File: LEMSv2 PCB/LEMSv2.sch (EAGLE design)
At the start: 82 parts, among them J1 FEMALE 2x3, Q1 200mA/50V, Q10 200mA/50V, Q2 200mA/50V, Q4 MMBT3904, Q5 200mA/50V, Q6 MMBT3904, Q7 200mA/50V, Q8 MMBT3904, Q9 MMBT3904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

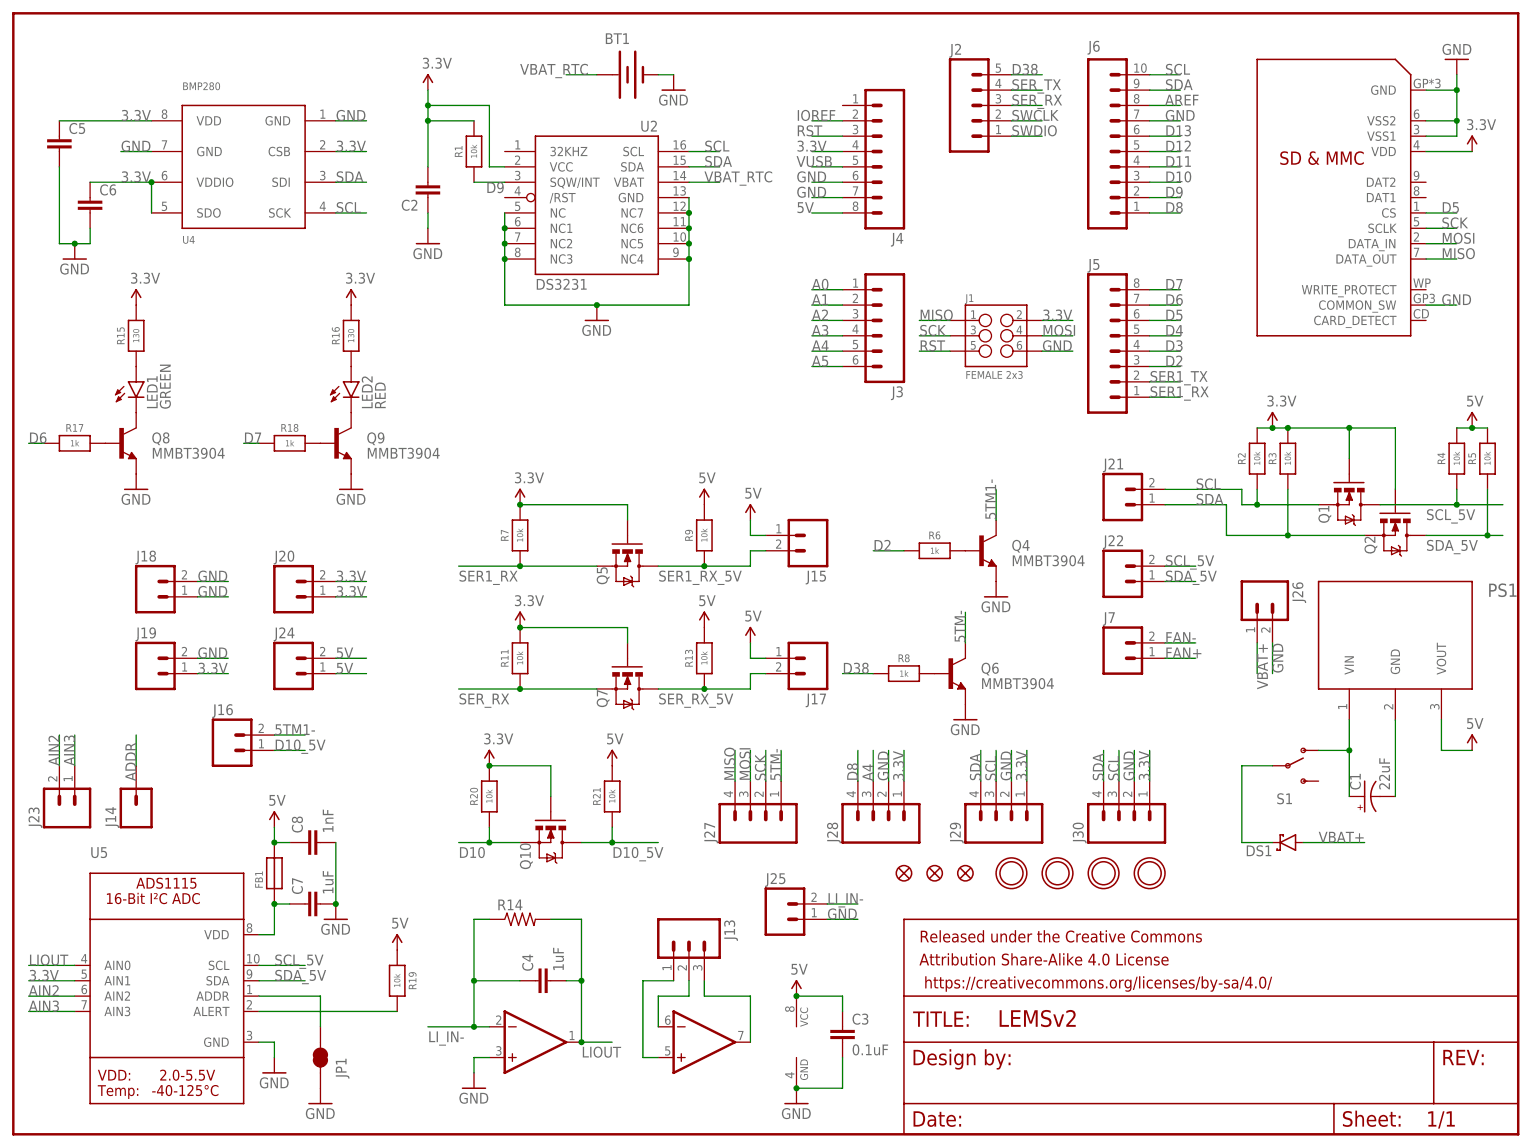
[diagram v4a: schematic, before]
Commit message: Started routing, part changes
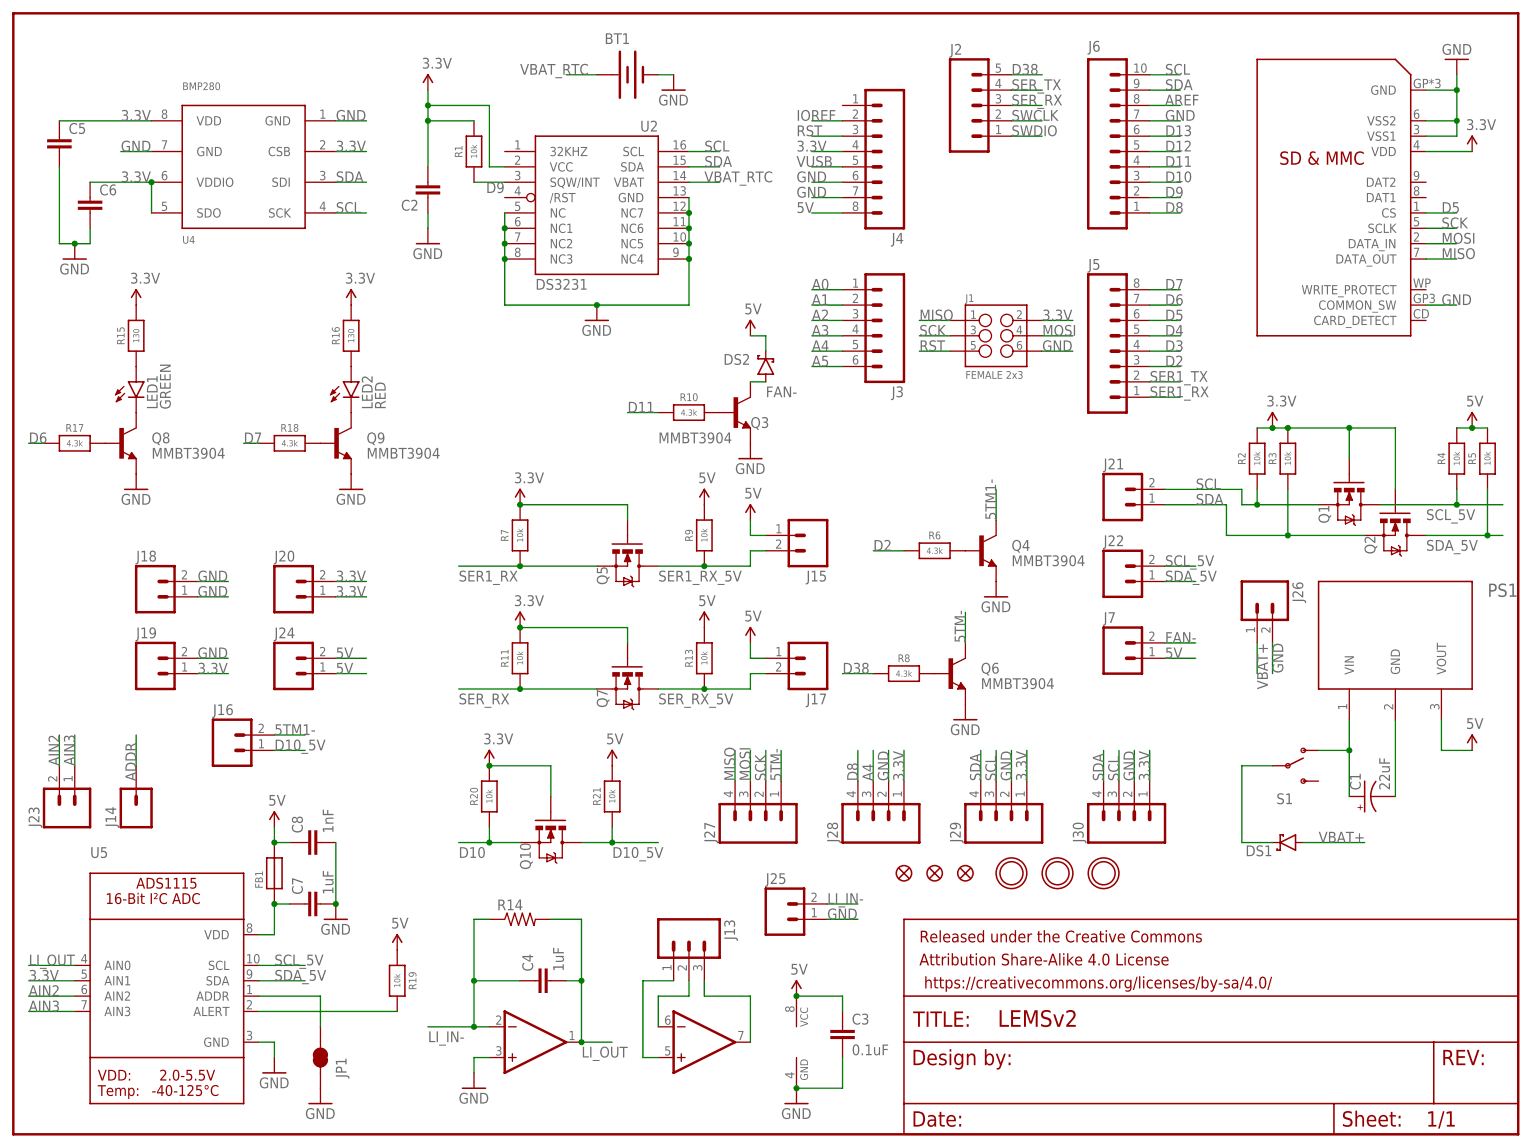
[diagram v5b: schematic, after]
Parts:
- removed U$4: MOUNTINGHOLE2.5, LEMSv2:MOUNTINGHOLE2.5
- added DS2: DIODE_SCHOTTKY, LEMSv2:DIODE_SCHOTTKY
- added Q3: MMBT3904, LEMSv2:MMBT3904
- added R10: 4.3k, LEMSv2:RESISTOR_0805
- R17, R18, R6, R8: value 1k -> 4.3k
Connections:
- net LIOUT renamed LI_OUT
- removed net FAN+: J7.1
- new net N$15: Q3.B, R10.2
- net 5V: now also DS2.C, J7.1
- net D11: now also R10.1
- net FAN-: now also DS2.A, Q3.C
- net GND: now also Q3.E
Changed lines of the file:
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@@
 <part name="U$2" library="LEMSv2" deviceset="MOUNTINGHOLE" device="2.5"/>
 <part name="U$3" library="LEMSv2" deviceset="MOUNTINGHOLE" device="2.5"/>
-<part name="U$4" library="LEMSv2" deviceset="MOUNTINGHOLE" device="2.5"/>
 <part name="C3" library="LEMSv2" deviceset="CAP" device="" value="0.1uF"/>
 <part name="U3" library="LEMSv2" deviceset="TLV2372" device=""/>
@@
 <part name="R15" library="LEMSv2" deviceset="RESISTOR" device="_0805" value="130"/>
 <part name="R16" library="LEMSv2" deviceset="RESISTOR" device="_0805" value="130"/>
-<part name="R17" library="LEMSv2" deviceset="RESISTOR" device="_0805" value="1k"/>
-<part name="R18" library="LEMSv2" deviceset="RESISTOR" device="_0805" value="1k"/>
+<part name="R17" library="LEMSv2" deviceset="RESISTOR" device="_0805" value="4.3k"/>
+<part name="R18" library="LEMSv2" deviceset="RESISTOR" device="_0805" value="4.3k"/>
 <part name="LED1" library="LEMSv2" deviceset="LED_GREEN" device="" value="GREEN"/>
 <part name="LED2" library="LEMSv2" deviceset="LED_RED" device="" value="RED"/>
@@
 <part name="Q4" library="LEMSv2" deviceset="MMBT3904" device=""/>
 <part name="Q6" library="LEMSv2" deviceset="MMBT3904" device=""/>
-<part name="R6" library="LEMSv2" deviceset="RESISTOR" device="_0805" value="1k"/>
-<part name="R8" library="LEMSv2" deviceset="RESISTOR" device="_0805" value="1k"/>
+<part name="R6" library="LEMSv2" deviceset="RESISTOR" device="_0805" value="4.3k"/>
+<part name="R8" library="LEMSv2" deviceset="RESISTOR" device="_0805" value="4.3k"/>
 <part name="SUPPLY17" library="LEMSv2" deviceset="5V" device=""/>
 <part name="SUPPLY18" library="LEMSv2" deviceset="5V" device=""/>
@@
 <part name="GND14" library="LEMSv2" deviceset="GND" device=""/>
 <part name="DS1" library="LEMSv2" deviceset="DIODE_SCHOTTKY" device=""/>
+<part name="DS2" library="LEMSv2" deviceset="DIODE_SCHOTTKY" device=""/>
+<part name="Q3" library="LEMSv2" deviceset="MMBT3904" device=""/>
+<part name="R10" library="LEMSv2" deviceset="RESISTOR" device="_0805" value="4.3k"/>
+<part name="GND15" library="LEMSv2" deviceset="GND" device=""/>
+<part name="SUPPLY19" library="LEMSv2" deviceset="5V" device=""/>
 </parts>
 <sheets>
@@
 <instance part="U$2" gate="G$1" x="172.72" y="43.18"/>
 <instance part="U$3" gate="G$1" x="180.34" y="43.18"/>
-<instance part="U$4" gate="G$1" x="187.96" y="43.18"/>
 <instance part="C3" gate="G$1" x="137.16" y="15.24"/>
 <instance part="U3" gate="TLV2372-1" x="83.82" y="15.24" smashed="yes"/>
@@
 <attribute name="NAME" x="208.28" y="47.7774" size="1.778" layer="95" rot="R180"/>
 </instance>
+<instance part="DS2" gate="G$1" x="124.46" y="127" smashed="yes" rot="R90">
+<attribute name="NAME" x="121.92" y="129.0574" size="1.778" layer="95" rot="R180"/>
+</instance>
+<instance part="Q3" gate="G$1" x="119.38" y="119.38" smashed="yes">
+<attribute name="NAME" x="121.92" y="116.84" size="1.778" layer="95"/>
+<attribute name="VALUE" x="106.68" y="114.3" size="1.778" layer="96"/>
+</instance>
+<instance part="R10" gate="G$1" x="111.76" y="119.38"/>
+<instance part="GND15" gate="1" x="121.92" y="111.76"/>
+<instance part="SUPPLY19" gate="G$1" x="121.92" y="132.08"/>
 </instances>
 <busses>
@@
 <label x="208.28" y="81.28" size="1.778" layer="95" rot="R270"/>
 </segment>
+<segment>
+<pinref part="Q3" gate="G$1" pin="E"/>
+<pinref part="GND15" gate="1" pin="GND"/>
+</segment>
 </net>
 <net name="SCK" class="0">
@@
 <wire x1="121.92" y1="81.28" x2="121.92" y2="78.74" width="0.1524" layer="91"/>
 <wire x1="121.92" y1="78.74" x2="124.46" y2="78.74" width="0.1524" layer="91"/>
+</segment>
+<segment>
+<pinref part="DS2" gate="G$1" pin="C"/>
+<wire x1="124.46" y1="129.54" x2="124.46" y2="132.08" width="0.1524" layer="91"/>
+<wire x1="124.46" y1="132.08" x2="121.92" y2="132.08" width="0.1524" layer="91"/>
+<pinref part="SUPPLY19" gate="G$1" pin="5V"/>
+</segment>
+<segment>
+<pinref part="J7" gate="G$1" pin="1"/>
+<wire x1="190.5" y1="78.74" x2="195.58" y2="78.74" width="0.1524" layer="91"/>
+<label x="190.5" y="78.74" size="1.778" layer="95"/>
 </segment>
 </net>
@@
 <label x="190.5" y="160.02" size="1.778" layer="95"/>
 </segment>
+<segment>
+<pinref part="R10" gate="G$1" pin="1"/>
+<wire x1="106.68" y1="119.38" x2="101.6" y2="119.38" width="0.1524" layer="91"/>
+<label x="101.6" y="119.38" size="1.778" layer="95"/>
+</segment>
 </net>
 <net name="D10" class="0">
@@
 </segment>
 </net>
-<net name="LIOUT" class="0">
+<net name="LI_OUT" class="0">
 <segment>
 <pinref part="U3" gate="TLV2372-1" pin="OUT"/>
@@
 <label x="190.5" y="81.28" size="1.778" layer="95"/>
 </segment>
-</net>
-<net name="FAN+" class="0">
-<segment>
-<pinref part="J7" gate="G$1" pin="1"/>
-<wire x1="190.5" y1="78.74" x2="195.58" y2="78.74" width="0.1524" layer="91"/>
-<label x="190.5" y="78.74" size="1.778" layer="95"/>
+<segment>
+<pinref part="Q3" gate="G$1" pin="C"/>
+<pinref part="DS2" gate="G$1" pin="A"/>
+<wire x1="121.92" y1="124.46" x2="124.46" y2="124.46" width="0.1524" layer="91"/>
+<label x="124.46" y="121.92" size="1.778" layer="95"/>
 </segment>
 </net>
@@
 </segment>
 </net>
+<net name="N$15" class="0">
+<segment>
+<pinref part="Q3" gate="G$1" pin="B"/>
+<pinref part="R10" gate="G$1" pin="2"/>
+</segment>
+</net>

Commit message: More routing
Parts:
- C2: value (none) -> 1uF
- C5, C6: value (none) -> 0.1uF
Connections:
- new net RST2: J1.5
- net 5TM-: now also J17.2; no longer J27.1
- net D11: no longer R10.1
- net D4: now also R10.1
- net RST: no longer J1.5
- net SER_RX_5V: now also J27.1; no longer J17.2
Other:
- moved on the sheet: J15, J17
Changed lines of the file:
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@@
 <part name="C1" library="LEMSv2" deviceset="CAP_POL" device="PTH2" value="22uF"/>
 <part name="SUPPLY2" library="SparkFun-Aesthetics" deviceset="5V" device=""/>
-<part name="C2" library="LEMSv2" deviceset="CAP" device=""/>
+<part name="C2" library="LEMSv2" deviceset="CAP" device="" value="1uF"/>
 <part name="GND1" library="LEMSv2" deviceset="GND" device=""/>
 <part name="SUPPLY3" library="LEMSv2" deviceset="3.3V" device=""/>
@@
 <part name="R14" library="adafruit" deviceset="R-US_" device="FLIPFLOP"/>
 <part name="U4" library="LEMSv2" deviceset="BMP280" device=""/>
-<part name="C5" library="LEMSv2" deviceset="CAP" device=""/>
-<part name="C6" library="LEMSv2" deviceset="CAP" device=""/>
+<part name="C5" library="LEMSv2" deviceset="CAP" device="" value="0.1uF"/>
+<part name="C6" library="LEMSv2" deviceset="CAP" device="" value="0.1uF"/>
 <part name="GND7" library="LEMSv2" deviceset="GND" device=""/>
 <part name="Q8" library="LEMSv2" deviceset="MMBT3904" device=""/>
@@
 <instance part="GND12" gate="1" x="50.8" y="5.08"/>
 <instance part="SUPPLY14" gate="G$1" x="63.5" y="30.48"/>
-<instance part="J15" gate="G$1" x="132.08" y="99.06" rot="R180"/>
+<instance part="J15" gate="G$1" x="132.08" y="96.52" rot="R180"/>
 <instance part="J16" gate="G$1" x="35.56" y="63.5"/>
-<instance part="J17" gate="G$1" x="132.08" y="78.74" rot="R180"/>
+<instance part="J17" gate="G$1" x="152.4" y="111.76" rot="R180"/>
 <instance part="J18" gate="G$1" x="22.86" y="88.9"/>
 <instance part="J19" gate="G$1" x="22.86" y="76.2"/>
@@
 <instance part="R6" gate="G$1" x="152.4" y="96.52"/>
 <instance part="R8" gate="G$1" x="147.32" y="76.2"/>
-<instance part="SUPPLY17" gate="G$1" x="121.92" y="101.6"/>
-<instance part="SUPPLY18" gate="G$1" x="121.92" y="81.28"/>
+<instance part="SUPPLY17" gate="G$1" x="124.46" y="99.06"/>
+<instance part="SUPPLY18" gate="G$1" x="142.24" y="111.76"/>
 <instance part="GND13" gate="1" x="162.56" y="88.9"/>
 <instance part="GND14" gate="1" x="157.48" y="68.58"/>
@@
 <label x="129.54" y="165.1" size="1.778" layer="95"/>
 </segment>
-<segment>
-<pinref part="J1" gate="G$1" pin="5"/>
-<wire x1="154.94" y1="129.54" x2="149.86" y2="129.54" width="0.1524" layer="91"/>
-<label x="149.86" y="129.54" size="1.778" layer="95"/>
-</segment>
 </net>
 <net name="VUSB" class="0">
@@
 <pinref part="SUPPLY17" gate="G$1" pin="5V"/>
 <pinref part="J15" gate="G$1" pin="1"/>
-<wire x1="121.92" y1="101.6" x2="121.92" y2="99.06" width="0.1524" layer="91"/>
-<wire x1="121.92" y1="99.06" x2="124.46" y2="99.06" width="0.1524" layer="91"/>
+<wire x1="124.46" y1="99.06" x2="124.46" y2="96.52" width="0.1524" layer="91"/>
 </segment>
 <segment>
 <pinref part="SUPPLY18" gate="G$1" pin="5V"/>
 <pinref part="J17" gate="G$1" pin="1"/>
-<wire x1="121.92" y1="81.28" x2="121.92" y2="78.74" width="0.1524" layer="91"/>
-<wire x1="121.92" y1="78.74" x2="124.46" y2="78.74" width="0.1524" layer="91"/>
+<wire x1="142.24" y1="111.76" x2="144.78" y2="111.76" width="0.1524" layer="91"/>
 </segment>
 <segment>
@@
 <label x="190.5" y="160.02" size="1.778" layer="95"/>
 </segment>
-<segment>
-<pinref part="R10" gate="G$1" pin="1"/>
-<wire x1="106.68" y1="119.38" x2="101.6" y2="119.38" width="0.1524" layer="91"/>
-<label x="101.6" y="119.38" size="1.778" layer="95"/>
-</segment>
 </net>
 <net name="D10" class="0">
@@
 <label x="190.5" y="132.08" size="1.778" layer="95"/>
 </segment>
+<segment>
+<pinref part="R10" gate="G$1" pin="1"/>
+<wire x1="106.68" y1="119.38" x2="101.6" y2="119.38" width="0.1524" layer="91"/>
+<label x="101.6" y="119.38" size="1.778" layer="95"/>
+</segment>
 </net>
 <net name="D3" class="0">
@@
 <wire x1="106.68" y1="93.98" x2="114.3" y2="93.98" width="0.1524" layer="91"/>
 <pinref part="R9" gate="G$1" pin="1"/>
-<wire x1="114.3" y1="93.98" x2="121.92" y2="93.98" width="0.1524" layer="91"/>
+<wire x1="114.3" y1="93.98" x2="124.46" y2="93.98" width="0.1524" layer="91"/>
 <junction x="114.3" y="93.98"/>
 <label x="106.68" y="91.44" size="1.778" layer="95"/>
-<wire x1="121.92" y1="93.98" x2="121.92" y2="96.52" width="0.1524" layer="91"/>
 <pinref part="J15" gate="G$1" pin="2"/>
-<wire x1="121.92" y1="96.52" x2="124.46" y2="96.52" width="0.1524" layer="91"/>
 </segment>
 </net>
@@
 <junction x="114.3" y="73.66"/>
 <label x="106.68" y="71.12" size="1.778" layer="95"/>
-<wire x1="121.92" y1="73.66" x2="121.92" y2="76.2" width="0.1524" layer="91"/>
-<pinref part="J17" gate="G$1" pin="2"/>
-<wire x1="121.92" y1="76.2" x2="124.46" y2="76.2" width="0.1524" layer="91"/>
+</segment>
+<segment>
+<pinref part="J27" gate="G$1" pin="1"/>
+<wire x1="127" y1="58.42" x2="127" y2="63.5" width="0.1524" layer="91"/>
+<label x="127" y="58.42" size="1.778" layer="95" rot="R90"/>
 </segment>
 </net>
@@
 <net name="D10_5V" class="0">
 <segment>
+<pinref part="J16" gate="G$1" pin="1"/>
+<wire x1="43.18" y1="63.5" x2="48.26" y2="63.5" width="0.1524" layer="91"/>
+<label x="43.18" y="63.5" size="1.778" layer="95"/>
+</segment>
+<segment>
 <pinref part="Q10" gate="G$1" pin="D"/>
 <wire x1="93.98" y1="48.26" x2="99.06" y2="48.26" width="0.1524" layer="91"/>
@@
 <label x="99.06" y="45.72" size="1.778" layer="95"/>
 </segment>
-<segment>
-<pinref part="J16" gate="G$1" pin="1"/>
-<wire x1="43.18" y1="63.5" x2="48.26" y2="63.5" width="0.1524" layer="91"/>
-<label x="43.18" y="63.5" size="1.778" layer="95"/>
-</segment>
 </net>
 <net name="FAN-" class="0">
@@
 </segment>
 <segment>
-<pinref part="J27" gate="G$1" pin="1"/>
-<wire x1="127" y1="58.42" x2="127" y2="63.5" width="0.1524" layer="91"/>
-<label x="127" y="58.42" size="1.778" layer="95" rot="R90"/>
+<pinref part="J17" gate="G$1" pin="2"/>
+<wire x1="144.78" y1="109.22" x2="139.7" y2="109.22" width="0.1524" layer="91"/>
+<label x="139.7" y="109.22" size="1.778" layer="95"/>
 </segment>
 </net>
@@
 </segment>
 </net>
+<net name="RST2" class="0">
+<segment>
+<pinref part="J1" gate="G$1" pin="5"/>
+<wire x1="154.94" y1="129.54" x2="149.86" y2="129.54" width="0.1524" layer="91"/>
+<label x="149.86" y="129.54" size="1.778" layer="95"/>
+</segment>
+</net>
